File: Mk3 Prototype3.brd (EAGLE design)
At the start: 119.6 x 68 mm, 153 parts, among them IC1 TPD3E001DRL, IC2 TPS62082, IC3 STM32F401V, IC4 BQ24092, IC6 CC3100MOD, IC7 BQ2970, IC8 LSM6DS3, IC9 LIS3MDL, J1 ZX62-AB-5PA(11), J2 ER-CON50HT-1, J3 SWD_SHROUD, Q1 DMMT5401, Q2 CSD25402Q3A, Q3 CSD13202Q2, Q4 CSD85301Q2, Q6 CSD25402Q3A, Q8 CSD13202Q2, SW1 JOYSTICK_MINI_MULTICOMP, U1 USD-SOCKET-SDIODM3AT_0011, U2 ER-TFT024-3, X2 DNP (16MHz-3.2-2.5), X3 ABS07-32.768KHZ-T

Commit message: copying switch between libs
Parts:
- S3, S4: device Mine:TACTILE_SWITCH_TALL -> TiLDA Mk3 Parts:TACTILE_SWITCH_TALL
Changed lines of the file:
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@@
 <?xml version="1.0" encoding="utf-8"?>
 <!DOCTYPE eagle SYSTEM "eagle.dtd">
-<eagle version="6.6.0">
+<eagle version="6.5.0">
 <drawing>
 <settings>
@@
 <attribute name="FARNELL" value="1316987" x="97.1" y="28.2" size="1.778" layer="27" rot="R135" display="off"/>
 </element>
-<element name="S4" library="Mine" package="TACTILE_SWITCH_TALL" value="1217769" x="25.2" y="32.4" smashed="yes" rot="R270">
+<element name="S4" library="TiLDA Mk3 Parts" package="TACTILE_SWITCH_TALL" value="1217769" x="25.2" y="32.4" smashed="yes" rot="R270">
 <attribute name="FARNELL" value="1217769" x="25.2" y="32.4" size="1.778" layer="27" rot="R270" display="off"/>
 </element>
-<element name="S3" library="Mine" package="TACTILE_SWITCH_TALL" value="1217769" x="16.2" y="24.8" smashed="yes" rot="R270">
+<element name="S3" library="TiLDA Mk3 Parts" package="TACTILE_SWITCH_TALL" value="1217769" x="16.2" y="24.8" smashed="yes" rot="R270">
 <attribute name="FARNELL" value="1217769" x="16.2" y="24.8" size="1.778" layer="27" rot="R270" display="off"/>
 </element>

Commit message: cc spi clk moved to allow dac, led fet moved, ws2812 on timer
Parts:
- moved Q3 30.1 mm to (13.2, 22.4)
- moved SG1 2.80 mm to (8.40, 47.6)
- moved R26 2.80 mm to (16.4, 43.4)
- moved C17 2.40 mm to (16.4, 41.6)
- moved U1 2.40 mm to (7.20, 35.6)
- turned D1 to 90 degrees
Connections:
- removed net TIM1_CH3: IC3.44, JP2.9
- new net BOOT1: IC3.37, R11.2
- new net DAC_OUT: IC3.30, JP2.5
- new net N$14: J2.44
- new net N$16: J2.47
- new net N$18: J2.46
- new net N$19: J2.45
- net ADC_IN: now also JP2.8; no longer JP2.7
- net SPI1_SCK: now also IC3.44; no longer IC3.30
- net TIM1_CH1N: now also IC3.64; no longer IC3.52
- net TIM1_CH2: now also JP2.9; no longer JP2.8
- net USART3_RX: now also JP2.7; no longer JP2.6
- net USART3_TX: now also JP2.6; no longer JP2.5
- net WS2812: now also IC3.52; no longer IC3.37, R11.2
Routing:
- net TIM1_CH1N: track 54.1 -> 12.9 mm, vias 6 -> 2
- net TIM1_CH3: track 22.8 -> 0.00 mm, vias 1 -> 0
- net DAC_OUT: track 0.00 -> 19.6 mm, vias 0 -> 1
- net SPI1_SCK: track 82.8 -> 93.5 mm, vias 2 -> 0
- net WS2812: track 18.1 -> 8.81 mm
- net BOOT1: track 0.00 -> 8.21 mm
- net JOY_DWN: track 0.00 -> 7.15 mm, vias 0 -> 1
- net BUZZ: track 29.8 -> 36.0 mm
- net FET_OUT: track 16.2 -> 10.8 mm
- net TIM1_CH4: track 24.4 -> 19.4 mm
- net N$21: track 40.8 -> 45.1 mm
- net +3V3: track 507.9 -> 504.7 mm
- net SDIO_CMD: track 28.7 -> 31.6 mm
- net SDIO_CLK: track 30.3 -> 32.9 mm
- net USB_ID: track 60.5 -> 63.1 mm
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
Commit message: sch mostly done for 0.3
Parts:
- removed C20, C21: DNP (0603/10p/50V/NP0), TiLDA Mk3 Parts:C0603K-SMALL
- removed R43: DNP (0603/150/5%), TiLDA Mk3 Parts:C0603K-SMALL
- removed X2: DNP (16MHz-3.2-2.5), TiLDA Mk3 Parts:CRYSTAL-3.2-2.5
- added S1: (no value), SparkFun-Electromechanical:TACTILE-SWITCH-1101NE
- added SJ2: JUMPER-PAD-3-2OF3_NC_BY_TRACE_SMALL, SparkFun-Passives:PAD-JUMPER-3-2OF3_NC_BY_TRACE_YES_SILK_FULL_BOX
- added TP2, TP3: TPB1,27, TiLDA Mk3 Parts:B1,27
- moved TP1 23.9 mm to (59.8, 38.8)
- moved C18 16.6 mm to (68.0, 16.2), turned to 180 degrees
- moved R3 14.6 mm to (71.4, 18.0)
- moved R4 14.2 mm to (69.7, 18.0)
- moved R18 10.4 mm to (64.0, 20.0), turned to 0 degrees
- moved TP19 9.14 mm to (52.4, 15.6)
- moved R19 7.88 mm to (62.4, 18.8), turned to 0 degrees
- moved C42 7.64 mm to (54.0, 20.8)
- moved C41 7.50 mm to (52.6, 20.8)
- moved C36 6.80 mm to (61.2, 26.0), turned to 90 degrees
- moved TP18 6.80 mm to (54.0, 16.8)
- moved IC9 4.94 mm to (56.4, 23.0), turned to 90 degrees
- moved C40 4.51 mm to (55.4, 20.0)
- moved R30 4.25 mm to (58.4, 22.0)
- moved L3 2.91 mm to (46.7, 16.9)
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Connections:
- removed net IMU_IRQ1: IC3.17, TP1.TP
- removed net N$14: J2.44
- removed net N$15: D3.C, Q1.5, Q2.5, Q2.6, Q2.7, Q2.8, Q2.EP, Q6.5, Q6.6, Q6.7, Q6.8, Q6.EP, R45.1
- removed net N$18: J2.46
- removed net N$19: J2.45
- removed net N$31: C21.2, IC3.12, X2.3
- removed net N$33: C20.2, R43.2, X2.1
- removed net N$42: IC3.13, R43.1
- new net ADC_X: IC3.17, J2.46
- new net ADC_Y: IC3.18, J2.47
- new net T_X: IC3.12, J2.44
- new net T_Y: IC3.13, J2.45
- net +3V3: now also SJ2.1
- net ADC_VIN: now also IC3.24; no longer IC3.18
- net GND: now also S1.2, SJ2.3; no longer C20.1, C21.1, X2.2, X2.4
- net LCD0: now also TP1.TP
- net LCD_MODE: now also SJ2.2
- net LCD_RD: now also TP2.TP
- net LCD_WRX: now also TP3.TP
- net N$16: now also D2.A, Q1.6, Q2.1, Q2.2, Q2.3, Q6.1, Q6.2, Q6.3; no longer J2.47
- net NRST: now also S1.1
- net SPI3_SCK: now also JP1.3, OUTLINE1.CH3
- net TIM2_CH2: no longer IC3.24, JP1.3, OUTLINE1.CH3
- net VBAT: now also Q6.5, Q6.6, Q6.7, Q6.8, Q6.EP, R45.1; no longer Q1.6, Q2.1, Q2.2, Q2.3
- net V_UNREG: now also D3.C, Q1.5, Q2.5, Q2.6, Q2.7, Q2.8, Q2.EP; no longer D2.A, Q6.1, Q6.2, Q6.3
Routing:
- net +3V3: track 504.7 -> 454.0 mm, vias 29 -> 28
- net TIM2_CH2: track 138.0 -> 100.9 mm
- net ADC_X: track 0.00 -> 27.4 mm
- net ADC_Y: track 0.00 -> 27.4 mm
- net T_X: track 0.00 -> 26.8 mm
- net T_Y: track 0.00 -> 26.7 mm
- net IMU_IRQ1: track 19.2 -> 0.00 mm
- net GND: track 146.5 -> 127.6 mm, vias 153 -> 145
- net IMU_SCL: track 26.5 -> 43.6 mm, vias 0 -> 2
- net ADC_VIN: track 57.3 -> 41.0 mm
- net IMU_SDA: track 26.3 -> 41.5 mm, vias 0 -> 2
- net VBUS: track 138.2 -> 123.5 mm
- net N$31: track 11.8 -> 0.00 mm
- net N$33: track 7.35 -> 0.00 mm
- net IMU_IRQ2: track 33.7 -> 26.7 mm
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
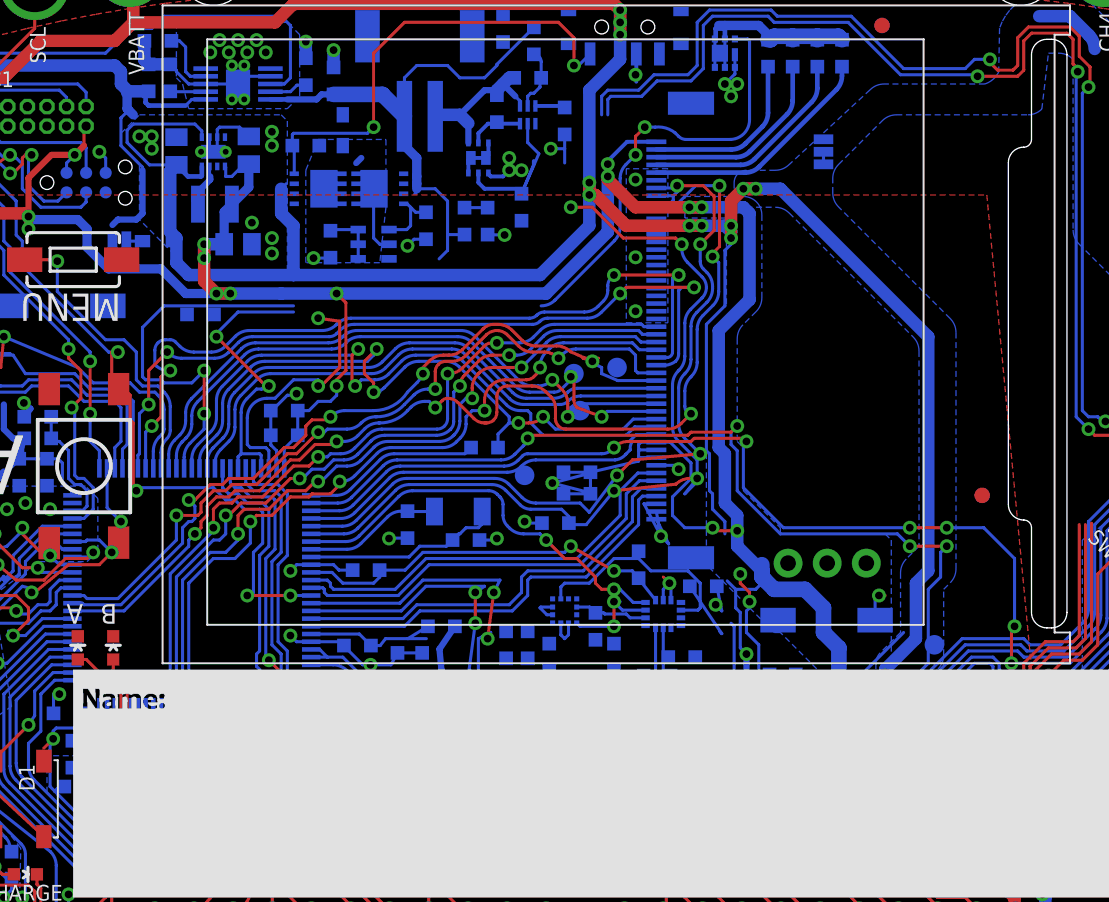
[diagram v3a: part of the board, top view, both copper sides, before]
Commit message: rearranged gpio, one gpio is now NC...
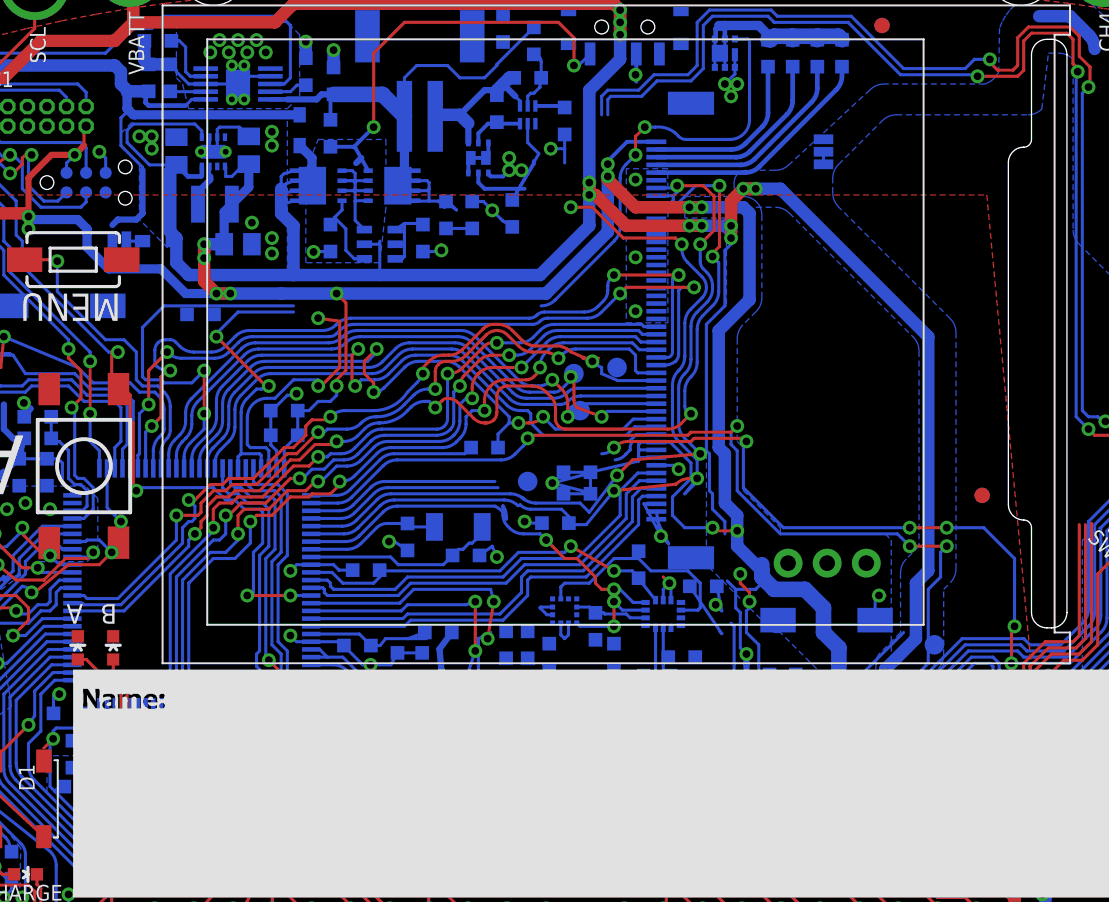
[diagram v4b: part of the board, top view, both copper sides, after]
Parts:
- moved R15 6.25 mm to (41.2, 47.2)
- moved R16 6.01 mm to (47.2, 47.2)
- moved Q6 4.80 mm to (45.2, 50.6)
- moved Q2 4.00 mm to (40.4, 50.6)
- moved D3 2.80 mm to (39.2, 54.2)
- moved R45 1.79 mm to (41.2, 54.0), turned to 270 degrees
- moved R21 1.26 mm to (48.7, 48.7), turned to 90 degrees
- moved R22 1.08 mm to (50.4, 48.7), turned to 90 degrees
- moved C24 1.00 mm to (50.0, 26.6)
- moved X3 1.00 mm to (49.5, 28.4)
- moved C23 0.80 mm to (46.2, 27.8)
- moved R28 0.72 mm to (53.0, 48.8)
- moved TP21 0.45 mm to (54.0, 31.4)
- moved R8 0.45 mm to (48.2, 21.6)
- moved Q1 0.40 mm to (44.4, 46.8), turned to 270 degrees
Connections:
- net ADC_VIN: now also IC3.26; no longer IC3.24
- net PB11: no longer C9.2, IC3.48
- net SPI3_SCK: no longer JP1.3, OUTLINE1.CH3
- net TIM2_CH2: now also IC3.24, JP1.3, OUTLINE1.CH3
- net TIM2_CH4: now also C9.2, IC3.48; no longer IC3.26
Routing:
- net ADC_VIN: track 41.0 -> 6.86 mm
- net TIM2_CH2: track 100.9 -> 135.0 mm
- net TIM2_CH4: track 150.8 -> 139.6 mm
- net VBUS: track 123.5 -> 134.3 mm
- net N$16: track 0.00 -> 10.1 mm
- net TEAR: track 25.5 -> 16.7 mm
- net CC_IRQ: track 92.2 -> 84.7 mm
- net V_UNREG: track 295.8 -> 302.9 mm
- net VBAT: track 35.5 -> 39.2 mm
- net GND: track 127.6 -> 130.7 mm
- net N$54: track 30.3 -> 27.3 mm
- net IMU_SDA: track 41.5 -> 39.1 mm
- net IMU_IRQ2: track 26.7 -> 28.6 mm
- net IMU_SCL: track 43.6 -> 42.1 mm
- net PB11: track 56.4 -> 54.9 mm
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
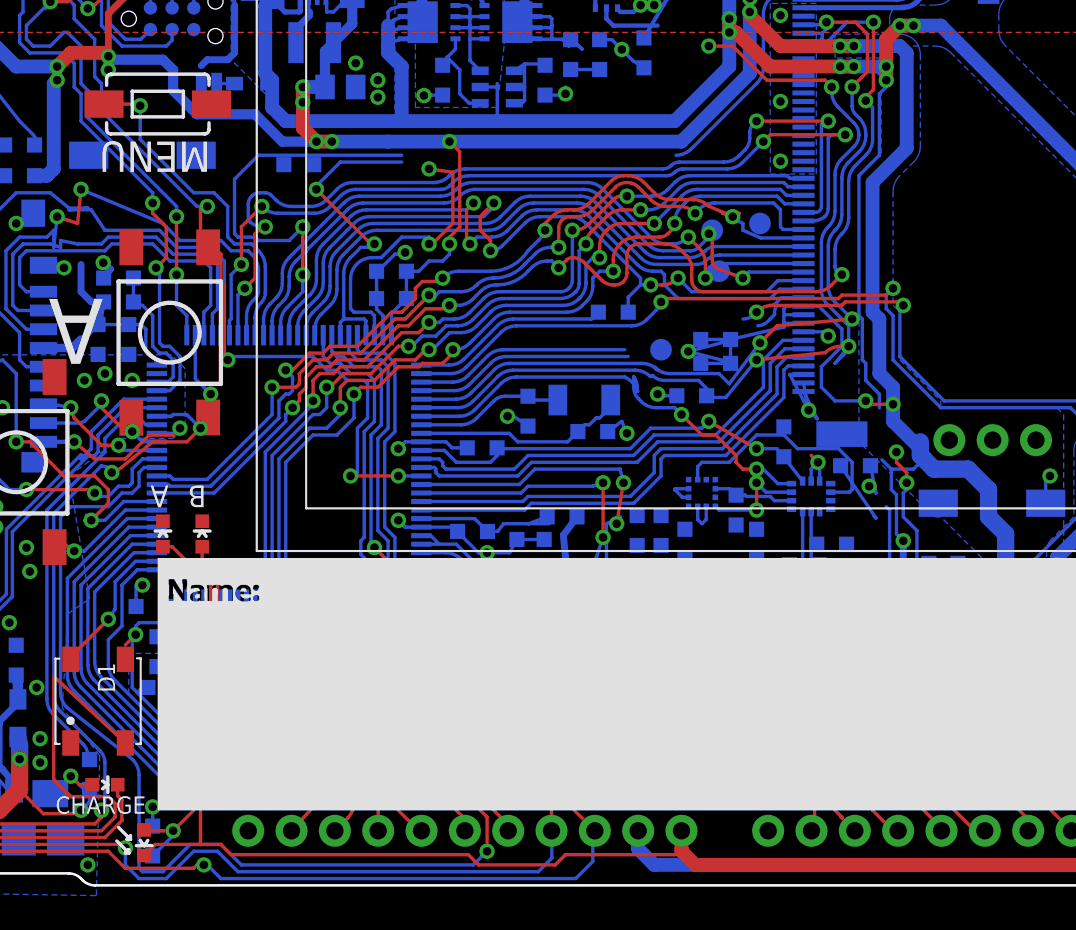
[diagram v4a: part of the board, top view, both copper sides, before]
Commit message: all gpio now connected
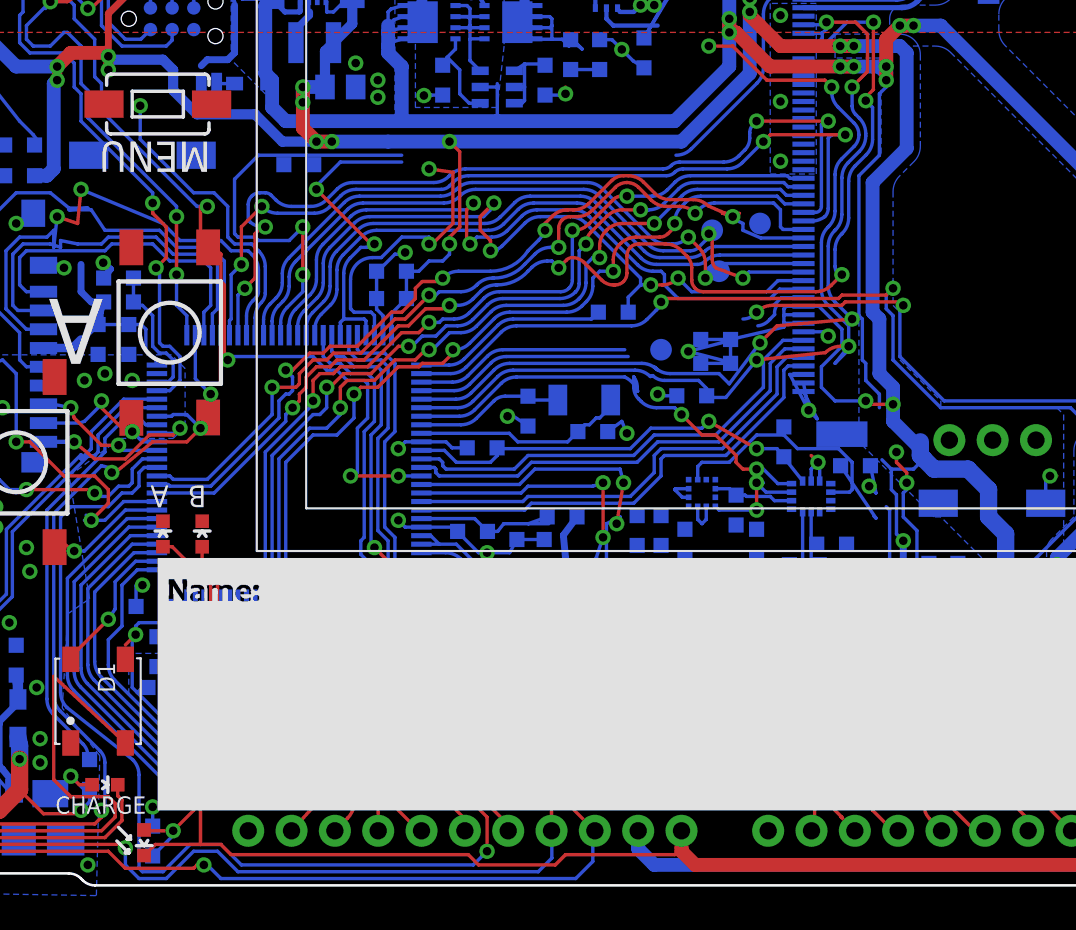
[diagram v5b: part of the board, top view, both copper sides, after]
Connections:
- net JOY_DWN renamed BTN_B
- removed net BOOT1: IC3.37, R11.2
- removed net MOM_DWN: IC3.56, SW1.B
- removed net MOM_RIGHT: IC3.55, SW1.A
- removed net PB11: JP1.7
- new net BTN_A: IC3.77, S4.B2
- new net JOY_DOWN: IC3.57, SW1.D
- new net JOY_RIGHTG: IC3.84
- new net PB2: IC3.37, JP1.7, R11.2
- net BTN_MENU: now also S7.2; no longer IC3.57, SW1.D
- net JOY_LEFT: now also IC3.56, SW1.B; no longer IC3.77, S4.B2
- net JOY_RIGHT: now also IC3.87, SW1.C; no longer IC3.84, S7.2
- net JOY_UP: now also IC3.55, SW1.A; no longer IC3.87, SW1.C
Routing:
- net JOY_DOWN: track 0.00 -> 103.5 mm, vias 0 -> 1
- net BTN_MENU: track 103.5 -> 0.00 mm, vias 1 -> 0
- net MOM_RIGHT: track 101.8 -> 0.00 mm, vias 1 -> 0
- net MOM_DWN: track 100.7 -> 0.00 mm, vias 1 -> 0
- net JOY_LEFT: track 5.26 -> 100.7 mm
- net JOY_RIGHT: track 20.0 -> 109.9 mm, vias 1 -> 5
- net PB2: track 0.00 -> 61.8 mm, vias 0 -> 3
- net PB11: track 54.9 -> 0.00 mm, vias 1 -> 0
- net TIM2_CH4: track 139.6 -> 169.1 mm, vias 4 -> 5
- net JOY_RIGHTG: track 0.00 -> 18.0 mm, vias 0 -> 1
- net BOOT1: track 8.21 -> 0.00 mm
- net JOY_UP: track 109.9 -> 101.8 mm, vias 5 -> 1
- net BTN_A: track 0.00 -> 5.26 mm, vias 0 -> 1
- net TIM2_CH2: track 135.0 -> 137.4 mm
- net SPI2_NSS: track 64.0 -> 65.5 mm
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
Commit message: routing intensifies...
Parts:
- removed SJ2: JUMPER-PAD-3-2OF3_NC_BY_TRACE_SMALL, SparkFun-Passives:PAD-JUMPER-3-2OF3_NC_BY_TRACE_YES_SILK_FULL_BOX
- moved C18 27.3 mm to (41.0, 12.0)
- moved TP19 5.25 mm to (57.4, 17.2)
- moved R31 4.75 mm to (58.4, 24.6), turned to 180 degrees
- moved TP18 3.94 mm to (57.4, 18.8)
- moved R18 3.30 mm to (60.8, 19.2), turned to 180 degrees
- moved C33 2.50 mm to (53.3, 28.6), turned to 90 degrees
- moved R19 1.84 mm to (64.2, 19.2)
- moved C36 1.22 mm to (61.0, 27.2)
- moved C41 1.00 mm to (52.0, 20.0)
- moved C42 1.00 mm to (53.4, 20.0)
- moved TP21 0.82 mm to (54.2, 32.2)
- moved R30 0.82 mm to (58.6, 21.2)
- moved IC8 0.80 mm to (62.8, 22.0)
- moved IC9 0.80 mm to (55.6, 23.0)
- moved C38 0.60 mm to (56.6, 32.0)
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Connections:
- removed net JOY_RIGHTG: IC3.84
- net +3V3: no longer SJ2.1
- net BTN_MENU: now also IC3.84
- net GND: no longer SJ2.3
- net LCD_MODE: no longer SJ2.2
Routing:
- net +3V3: track 453.6 -> 505.7 mm, vias 28 -> 27
- net BOOT0: track 101.3 -> 137.9 mm
- net ADC_VIN: track 6.86 -> 40.1 mm
- net BTN_MENU: track 0.00 -> 21.2 mm, vias 0 -> 1
- net V_UNREG: track 302.9 -> 284.3 mm
- net JOY_RIGHTG: track 18.0 -> 0.00 mm, vias 1 -> 0
- net TIM17_CH1: track 45.1 -> 61.7 mm
- net JOY_RIGHT: track 109.9 -> 122.4 mm
- net IMU_SCL: track 42.1 -> 32.7 mm
- net VBATT_IN: track 57.2 -> 66.4 mm
- net TEAR: track 16.7 -> 25.1 mm
- net IMU_SDA: track 39.1 -> 31.4 mm
- net USART1_TX: track 101.5 -> 96.1 mm
- net CC_IRQ: track 84.7 -> 90.0 mm
- net USART1_RX: track 104.8 -> 99.8 mm
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
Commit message: getting there
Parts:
- removed FID2, FID5: FIDUCIAL1X2.5-STOP, TiLDA Mk3 Parts:FIDUCIAL-1X2.5-STOP
- moved FID3 42.0 mm to (2.00, 8.00)
- moved FID1 10.3 mm to (83.0, 52.6)
- moved FID6 10.3 mm to (83.0, 52.6)
- moved R2 7.16 mm to (4.00, 10.0), turned to 0 degrees
- moved LED1 3.30 mm to (10.6, 16.2)
- moved R1 3.22 mm to (6.60, 16.3)
- moved ANT1 2.40 mm to (106.9, 1.60)
- moved FID4 1.20 mm to (1.90, 8.10)
- moved R31 0.63 mm to (58.6, 24.0)
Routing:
- net +3V3: track 505.7 -> 575.4 mm, vias 27 -> 31
- net FET_OUT: track 10.8 -> 70.0 mm, vias 1 -> 0
- net N$9: track 101.4 -> 59.9 mm, vias 2 -> 1
- net VBUS: track 134.3 -> 110.8 mm
- net ADC_VIN: track 40.1 -> 55.2 mm, vias 2 -> 4
- net V_UNREG: track 284.3 -> 299.2 mm, vias 17 -> 20
- net N$60: track 0.00 -> 14.7 mm
- net JOY_RIGHT: track 122.4 -> 113.5 mm, vias 5 -> 4
- net JOY_DOWN: track 103.5 -> 110.2 mm
- net BOOT0: track 137.9 -> 131.8 mm, vias 5 -> 4
- net USART1_RX: track 99.8 -> 105.3 mm
- net USART1_TX: track 96.1 -> 100.7 mm
- net USB_ID: track 63.1 -> 58.9 mm
- net I2C_SCL: track 160.0 -> 155.9 mm
- net TIM2_CH2: track 133.8 -> 137.7 mm
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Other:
- board size 119.6 x 68 mm -> 121.6 x 70 mm

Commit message: some more routing
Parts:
- moved C2 16.2 mm to (8.80, 14.0)
- moved SJ1 13.5 mm to (38.7, 54.6)
- moved D2 12.7 mm to (40.6, 54.0), turned to 90 degrees
- moved D3 11.1 mm to (30.6, 47.2), turned to 180 degrees
- moved LED4 1.34 mm to (24.9, 1.90), turned to 180 degrees
- moved R15 1.17 mm to (40.6, 48.2), turned to 0 degrees
- moved C4 1.13 mm to (9.20, 10.5)
- moved R10 0.82 mm to (21.3, 6.30)
- moved R45 0.80 mm to (42.0, 54.0)
- moved JP4 0.60 mm to (22.8, 50.2)
- moved C7 0.40 mm to (16.6, 13.2)
- moved IC1 0.40 mm to (14.4, 8.80)
- moved L2 0.40 mm to (16.7, 9.80)
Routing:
- net N$21: track 46.2 -> 35.1 mm
- net N$16: track 10.1 -> 14.7 mm
- net V_UNREG: track 299.2 -> 296.0 mm
- net USB_ID: track 58.9 -> 61.1 mm
- net SWDAT: track 57.8 -> 59.4 mm
- net D_P: track 31.6 -> 30.1 mm
- net SWCLK: track 46.2 -> 47.6 mm
- net GND: track 133.6 -> 132.3 mm
- net FET_OUT: track 70.0 -> 68.7 mm
- net +3V3: track 575.4 -> 574.1 mm, vias 31 -> 30
- net N$8: track 24.2 -> 25.0 mm
- net CC_HIB: track 130.9 -> 130.1 mm
- net N$54: track 26.2 -> 25.4 mm
- net WS2812: track 8.81 -> 9.56 mm
- net SPI2_NSS: track 65.5 -> 64.8 mm
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- removed copper zone on layer 16, net N$15
